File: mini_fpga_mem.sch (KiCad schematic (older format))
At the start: 52 parts, among them U3 XC6SLX9, U4 IS43R86400D-6TL

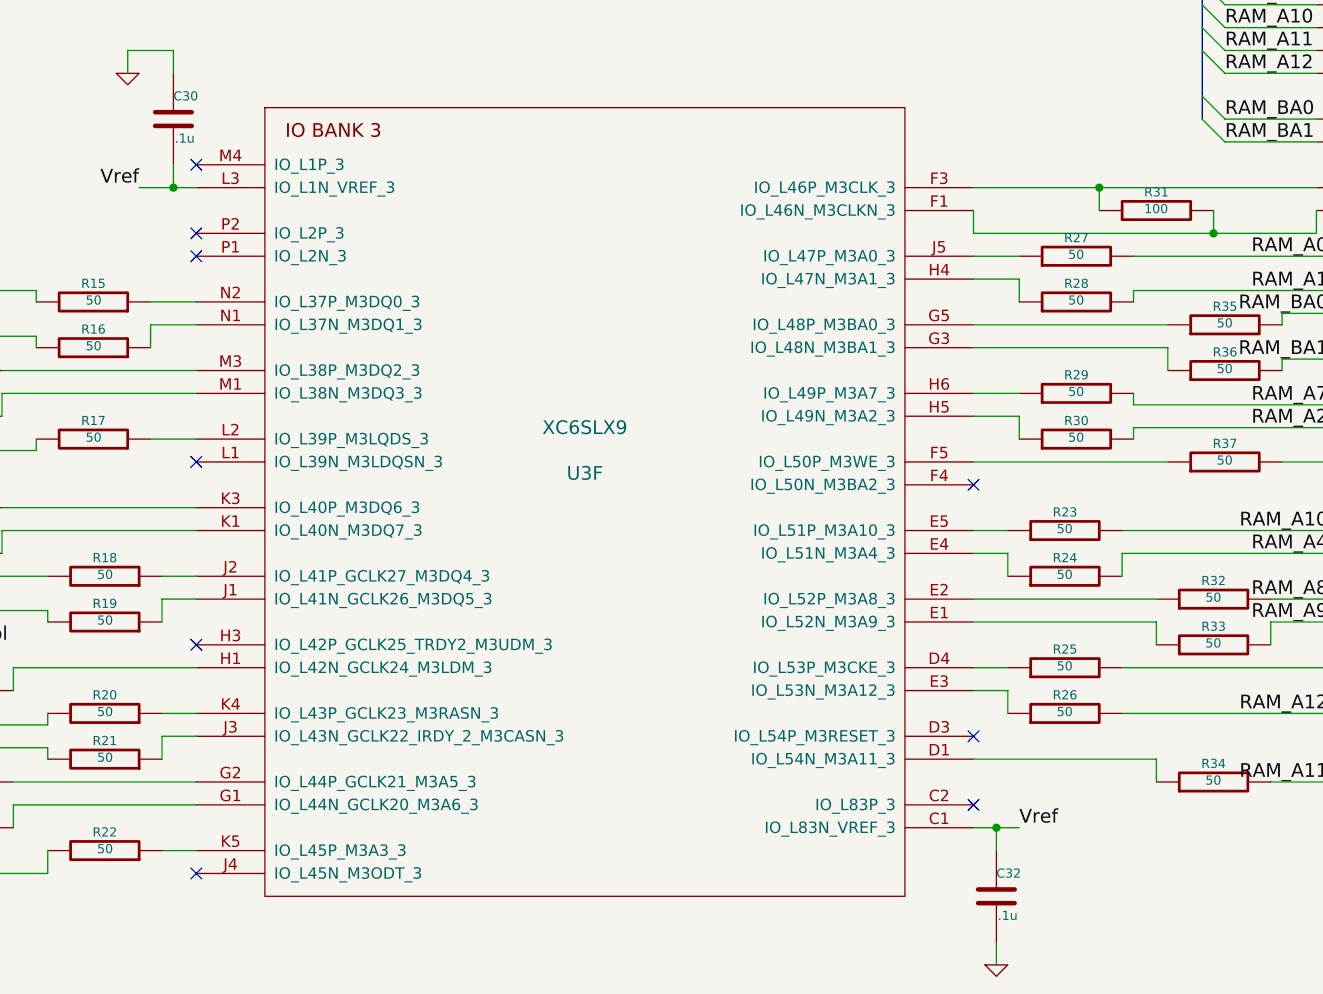
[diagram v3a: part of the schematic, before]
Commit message: Started routing DDR again using proper trace widths.
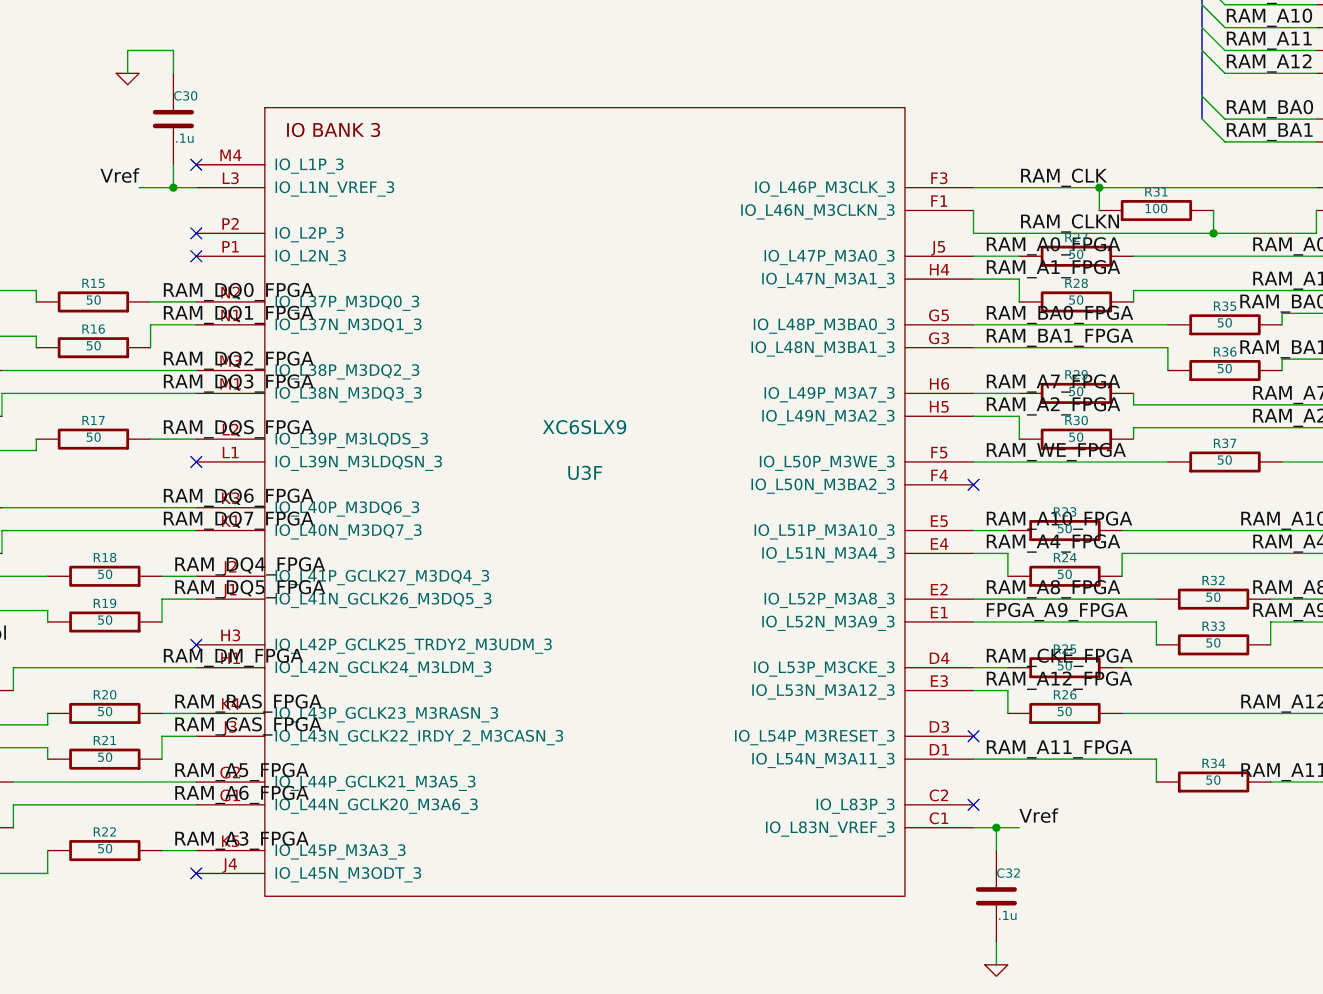
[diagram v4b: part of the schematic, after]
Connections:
- net RAM_A11_FPGA: now reaches R34.1, U3.D1 (IO_L54N_M3A11_3)
- net RAM_CKE_FPGA: now reaches R25.1, U3.D4 (IO_L53P_M3CKE_3)
- net FPGA_A9_FPGA: now reaches R33.1, U3.E1 (IO_L52N_M3A9_3)
- net RAM_A8_FPGA: now reaches R32.1, U3.E2 (IO_L52P_M3A8_3)
- net RAM_A12_FPGA: now reaches R26.1, U3.E3 (IO_L53N_M3A12_3)
- net RAM_A4_FPGA: now reaches R24.1, U3.E4 (IO_L51N_M3A4_3)
- net RAM_A10_FPGA: now reaches R23.1, U3.E5 (IO_L51P_M3A10_3)
- net RAM_CLKN: now reaches R31.2, U3.F1 (IO_L46N_M3CLKN_3), U4.46 (~CK~)
- net RAM_CLK: now reaches R31.1, U3.F3 (IO_L46P_M3CLK_3), U4.45 (CK)
- net RAM_WE_FPGA: now reaches R37.1, U3.F5 (IO_L50P_M3WE_3)
- net RAM_A6_FPGA: now reaches R14.1, U3.G1 (IO_L44N_GCLK20_M3A6_3)
- net RAM_A5_FPGA: now reaches R13.1, U3.G2 (IO_L44P_GCLK21_M3A5_3)
- net RAM_BA1_FPGA: now reaches R36.1, U3.G3 (IO_L48N_M3BA1_3)
- net RAM_BA0_FPGA: now reaches R35.1, U3.G5 (IO_L48P_M3BA0_3)
- net RAM_DM_FPGA: now reaches R12.1, U3.H1 (IO_L42N_GCLK24_M3LDM_3)
- net RAM_A1_FPGA: now reaches R28.1, U3.H4 (IO_L47N_M3A1_3)
- net RAM_A2_FPGA: now reaches R30.1, U3.H5 (IO_L49N_M3A2_3)
- net RAM_A7_FPGA: now reaches R29.1, U3.H6 (IO_L49P_M3A7_3)
- net RAM_DQ5_FPGA: now reaches R19.1, U3.J1 (IO_L41N_GCLK26_M3DQ5_3)
- net RAM_DQ4_FPGA: now reaches R18.1, U3.J2 (IO_L41P_GCLK27_M3DQ4_3)
- net RAM_CAS_FPGA: now reaches R21.1, U3.J3 (IO_L43N_GCLK22_IRDY_2_M3CASN_3)
- net RAM_A0_FPGA: now reaches R27.1, U3.J5 (IO_L47P_M3A0_3)
- net RAM_DQ7_FPGA: now reaches R11.1, U3.K1 (IO_L40N_M3DQ7_3)
- net RAM_DQ6_FPGA: now reaches R10.1, U3.K3 (IO_L40P_M3DQ6_3)
- net RAM_RAS_FPGA: now reaches R20.1, U3.K4 (IO_L43P_GCLK23_M3RASN_3)
- net RAM_A3_FPGA: now reaches R22.1, U3.K5 (IO_L45P_M3A3_3)
- net RAM_DQS_FPGA: now reaches R17.1, U3.L2 (IO_L39P_M3LQDS_3)
- net RAM_DQ3_FPGA: now reaches R9.1, U3.M1 (IO_L38N_M3DQ3_3)
- net RAM_DQ2_FPGA: now reaches R8.1, U3.M3 (IO_L38P_M3DQ2_3)
- net RAM_DQ1_FPGA: now reaches R16.1, U3.N1 (IO_L37N_M3DQ1_3)
- net RAM_DQ0_FPGA: now reaches R15.1, U3.N2 (IO_L37P_M3DQ0_3)
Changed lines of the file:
@@
 Sheet 3 6
 Title ""
-Date "3 aug 2014"
+Date "5 aug 2014"
 Rev ""
 Comp ""
@@
 Wire Wire Line
 	8150 1800 8150 1700
+Text Label 1950 4550 0    60   ~ 0
+RAM_DQ0_FPGA
+Text Label 1950 4650 0    60   ~ 0
+RAM_DQ1_FPGA
+Text Label 1950 4850 0    60   ~ 0
+RAM_DQ2_FPGA
+Text Label 1950 4950 0    60   ~ 0
+RAM_DQ3_FPGA
+Text Label 1950 5150 0    60   ~ 0
+RAM_DQS_FPGA
+Text Label 1950 5450 0    60   ~ 0
+RAM_DQ6_FPGA
+Text Label 1950 5550 0    60   ~ 0
+RAM_DQ7_FPGA
+Text Label 2000 5750 0    60   ~ 0
+RAM_DQ4_FPGA
+Text Label 2000 5850 0    60   ~ 0
+RAM_DQ5_FPGA
+Text Label 1950 6150 0    60   ~ 0
+RAM_DM_FPGA
+Text Label 2000 6350 0    60   ~ 0
+RAM_RAS_FPGA
+Text Label 2000 6450 0    60   ~ 0
+RAM_CAS_FPGA
+Text Label 2000 6650 0    60   ~ 0
+RAM_A5_FPGA
+Text Label 2000 6750 0    60   ~ 0
+RAM_A6_FPGA
+Text Label 2000 6950 0    60   ~ 0
+RAM_A3_FPGA
+Text Label 5700 4050 0    60   ~ 0
+RAM_CLK
+Text Label 5700 4250 0    60   ~ 0
+RAM_CLKN
+Text Label 5550 4350 0    60   ~ 0
+RAM_A0_FPGA
+Text Label 5550 4450 0    60   ~ 0
+RAM_A1_FPGA
+Text Label 5550 4650 0    60   ~ 0
+RAM_BA0_FPGA
+Text Label 5550 4750 0    60   ~ 0
+RAM_BA1_FPGA
+Text Label 5550 4950 0    60   ~ 0
+RAM_A7_FPGA
+Text Label 5550 5050 0    60   ~ 0
+RAM_A2_FPGA
+Text Label 5550 5250 0    60   ~ 0
+RAM_WE_FPGA
+Text Label 5550 5550 0    60   ~ 0
+RAM_A10_FPGA
+Text Label 5550 5650 0    60   ~ 0
+RAM_A4_FPGA
+Text Label 5550 5850 0    60   ~ 0
+RAM_A8_FPGA
+Text Label 5550 5950 0    60   ~ 0
+FPGA_A9_FPGA
+Text Label 5550 6150 0    60   ~ 0
+RAM_CKE_FPGA
+Text Label 5550 6250 0    60   ~ 0
+RAM_A12_FPGA
+Text Label 5550 6550 0    60   ~ 0
+RAM_A11_FPGA
 $EndSCHEMATC
